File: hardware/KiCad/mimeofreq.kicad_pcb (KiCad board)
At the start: 4 copper layers, 60 x 70 mm, 45 parts, among them J1 AudioJack2, J2 AudioJack2, J3 Jack-DC, SW1 SW_SPST, SW2 SW_SPST, SW3 SW_SPDT, U1 MCP6022, U2 MCP6022

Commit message: Adding op amps to board; bypass cap correction.
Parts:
- moved C8 106.3 mm to (151.0, 85.2)
- moved U2 98.6 mm to (140.2, 85.2)
- moved U1 87.9 mm to (140.2, 63.7)
- moved C4 85.4 mm to (151.0, 63.7)
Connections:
- C4 pad 2: Net-(U1C-V+) -> GND
- C8 pad 2: Net-(U2C-V+) -> GND
- U1 pad 8: Net-(U1C-V+) -> +3V3
- U2 pad 8: Net-(U2C-V+) -> +3V3
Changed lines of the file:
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@@
 	(footprint "Capacitor_THT_Custom:C_Rect_L4.0mm_W2.6mm_P2.50mm"
 		(layer "F.Cu")
-		(at 52.7941 125.9156)
+		(at 151 85.19)
 		(descr "C, Rect series, Radial; Designed for K104x15X7RF5xxx 0.1uF X7R ceramic capacitor.")
 		(tags "K104K15X7RF5TL2 ")
@@
 			(layers "*.Cu" "*.Mask")
 			(remove_unused_layers no)
-			(net "Net-(U2C-V+)")
+			(net "GND")
 			(pintype "passive")
 		)
@@
 	(footprint "Package_DIP:DIP-8_W7.62mm"
 		(layer "F.Cu")
-		(at 71.225 118.175)
+		(at 140.195 63.69)
 		(descr "8-lead though-hole mounted DIP package, row spacing 7.62mm (300 mils)")
 		(tags "THT DIP DIL PDIP 2.54mm 7.62mm 300mil")
@@
 		)
 		(point
-			(at 75.035 121.985)
+			(at 144.005 67.5)
 			(size 1.27)
 			(layer "F.Fab")
@@
 			(layers "*.Cu" "*.Mask")
 			(remove_unused_layers no)
-			(net "Net-(U1C-V+)")
+			(net "+3V3")
 			(pinfunction "V+_8")
 			(pintype "power_in")
@@
 	(footprint "Capacitor_THT_Custom:C_Rect_L4.0mm_W2.6mm_P2.50mm"
 		(layer "F.Cu")
-		(at 76.8641 106.1056)
+		(at 151 63.7)
 		(descr "C, Rect series, Radial; Designed for K104x15X7RF5xxx 0.1uF X7R ceramic capacitor.")
 		(tags "K104K15X7RF5TL2 ")
@@
 			(layers "*.Cu" "*.Mask")
 			(remove_unused_layers no)
-			(net "Net-(U1C-V+)")
+			(net "GND")
 			(pintype "passive")
 		)
@@
 	(footprint "Package_DIP:DIP-8_W7.62mm"
 		(layer "F.Cu")
-		(at 43.855 106.025)
+		(at 140.195 85.19)
 		(descr "8-lead though-hole mounted DIP package, row spacing 7.62mm (300 mils)")
 		(tags "THT DIP DIL PDIP 2.54mm 7.62mm 300mil")
@@
 		)
 		(point
-			(at 47.665 109.835)
+			(at 144.005 89)
 			(size 1.27)
 			(layer "F.Fab")
@@
 			(layers "*.Cu" "*.Mask")
 			(remove_unused_layers no)
-			(net "Net-(U2C-V+)")
+			(net "+3V3")
 			(pinfunction "V+_8")
 			(pintype "power_in")

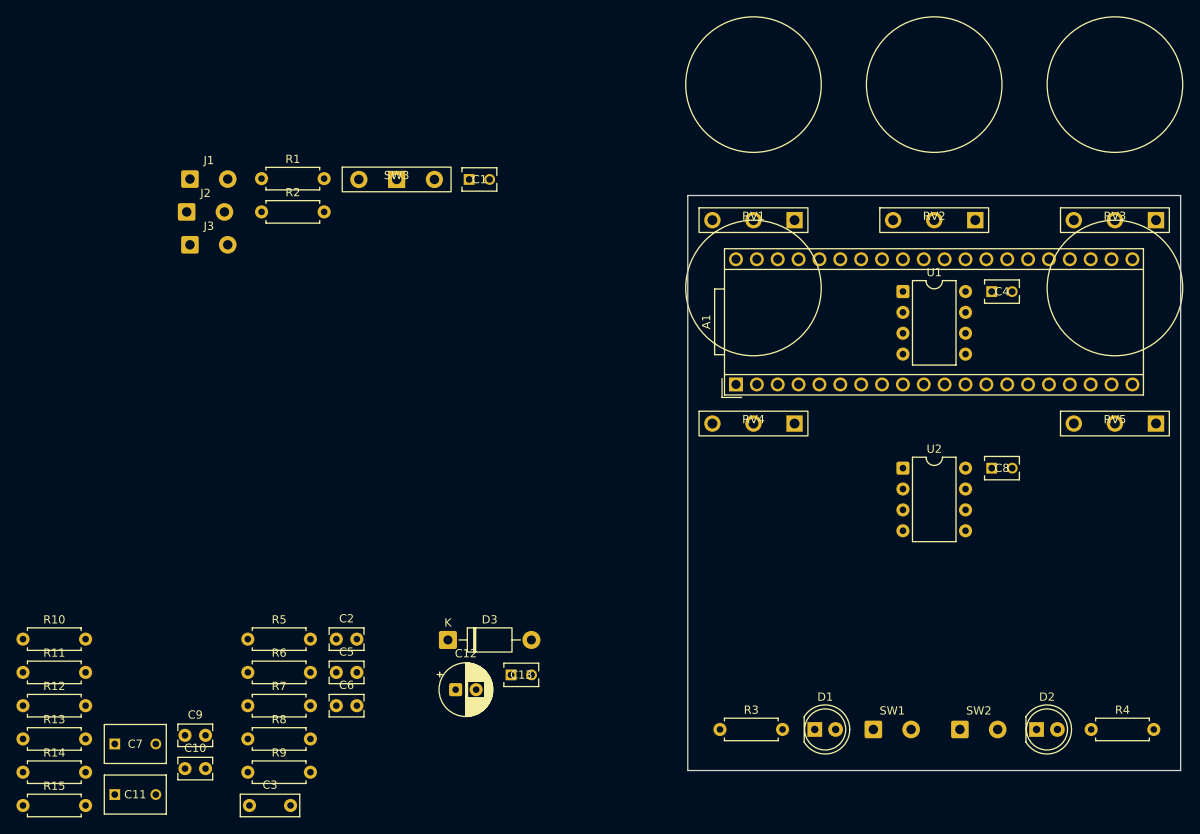
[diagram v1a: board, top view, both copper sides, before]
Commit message: Initial resistor board placement.
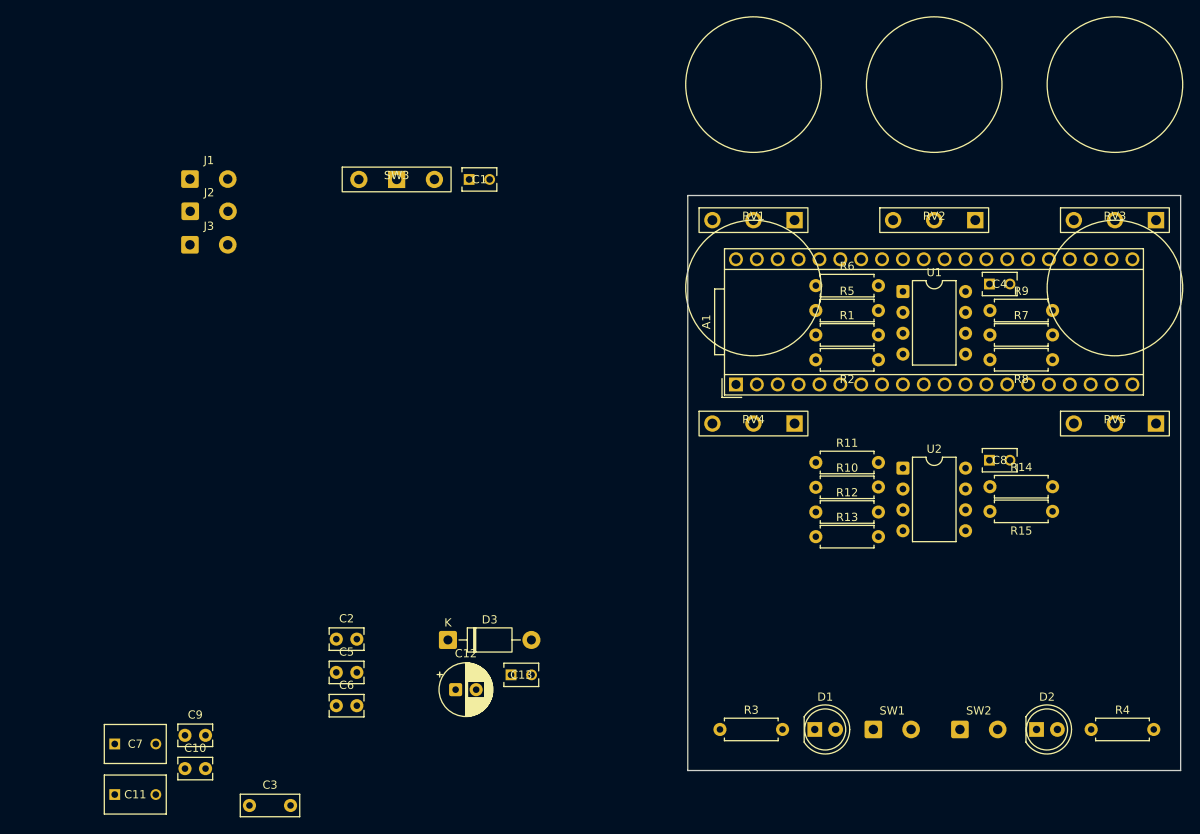
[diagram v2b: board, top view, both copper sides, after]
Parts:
- moved R15 130.3 mm to (158.4, 90.5), turned to 180 degrees
- moved R14 122.7 mm to (150.8, 87.5)
- moved R8 108.3 mm to (158.4, 72.0), turned to 180 degrees
- moved R9 106.4 mm to (150.8, 66.0)
- moved R7 101.0 mm to (150.8, 69.0)
- moved R11 99.8 mm to (129.6, 84.5)
- moved R13 99.6 mm to (129.6, 93.5)
- moved R12 99.4 mm to (129.6, 90.5)
- moved R10 98.3 mm to (129.6, 87.5)
- moved R6 83.7 mm to (129.6, 63.0)
- moved R5 79.9 mm to (129.6, 66.0)
- moved R2 77.2 mm to (137.2, 72.0), turned to 180 degrees
- moved R1 70.1 mm to (129.6, 69.0)
- moved C8 1.00 mm to (150.7, 84.2)
- moved C4 0.97 mm to (150.7, 62.8)
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
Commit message: All components fit on PCB. Some footprints replaced.
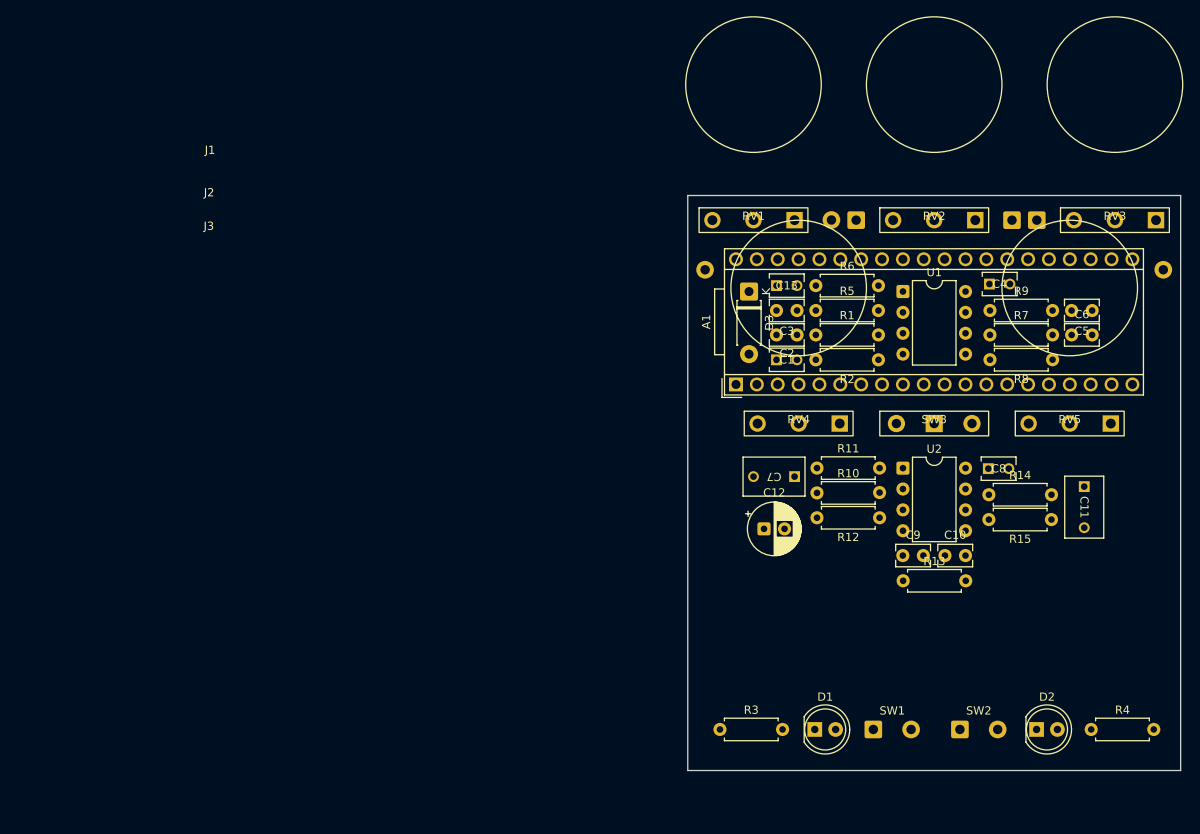
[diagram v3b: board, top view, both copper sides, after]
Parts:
- C3: footprint Capacitor_THT:C_Rect_L7.0mm_W2.5mm_P5.00mm -> Capacitor_THT:C_Rect_L4.0mm_W2.5mm_P2.50mm
- D3: footprint Diode_THT:D_DO-41_SOD81_P10.16mm_Horizontal -> Diode_THT:D_DO-41_SOD81_P7.62mm_Horizontal
- moved C11 123.8 mm to (162.3, 87.4), turned to -90 degrees
- moved C5 102.0 mm to (163.2, 66.0), turned to 180 degrees
- moved C6 100.3 mm to (160.7, 69.0)
- moved C10 96.1 mm to (145.3, 95.8)
- moved C9 90.1 mm to (140.2, 95.8)
- moved C3 89.9 mm to (127.3, 66.0), turned to 180 degrees
- moved C7 88.9 mm to (127.0, 86.2), turned to 180 degrees
- moved SW3 71.9 mm to (144.0, 79.8)
- moved C2 65.1 mm to (124.8, 69.0)
- moved C13 57.4 mm to (124.8, 63.0)
- moved D3 56.1 mm to (121.5, 63.7), turned to -90 degrees
- moved C1 43.4 mm to (124.8, 72.0)
- moved C12 42.3 mm to (123.3, 92.6)
- moved R13 11.9 mm to (140.2, 98.9)
- moved R12 7.79 mm to (137.3, 91.2), turned to 180 degrees
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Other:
- copper layers 4 -> 2

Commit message: Upper half initial routing.
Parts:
- moved R4 10.0 mm to (163.0, 107.0)
- moved D1 10.0 mm to (129.5, 107.0)
- moved D2 10.0 mm to (156.5, 107.0)
- moved R3 10.0 mm to (117.9, 107.0)
- moved SW1 10.0 mm to (136.6, 107.0)
- moved SW2 10.0 mm to (147.1, 107.0)
- moved R2 7.62 mm to (129.6, 72.0), turned to 0 degrees
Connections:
- A1 pad 22: /POT1 -> /POT5
- A1 pad 23: /POT2 -> /POT4
- A1 pad 25: /POT4 -> /POT2
- A1 pad 26: /POT5 -> /POT1
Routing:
- net +3V3: track 0.00 -> 189.2 mm
- net /POT4: track 0.00 -> 47.9 mm
- net +9VCLEAN: track 0.00 -> 45.6 mm
- net /POT1: track 0.00 -> 38.6 mm
- net +9V: track 0.00 -> 28.4 mm
- net /POT5: track 0.00 -> 22.1 mm
- net Net-(R6-Pad2): track 0.00 -> 16.8 mm
- net Net-(U1B-+): track 0.00 -> 16.7 mm
- net Net-(U1B--): track 0.00 -> 16.5 mm
- net /POT2: track 0.00 -> 15.9 mm
- net VGND: track 0.00 -> 14.2 mm
- net /Input Buffer/JACK_IN: track 0.00 -> 13.7 mm
- net Net-(U1A--): track 0.00 -> 12.0 mm
- net /IN: track 0.00 -> 9.75 mm
- net Net-(C5-Pad1): track 0.00 -> 9.07 mm
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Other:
- board size 60 x 70 mm -> 60 x 60 mm

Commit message: Full board initial routing.
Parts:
- moved D1 2.61 mm to (132.1, 107.0), turned to 180 degrees
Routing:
- net /LED2: track 0.00 -> 65.7 mm
- net /FS2: track 0.00 -> 55.1 mm
- net /OUT: track 0.00 -> 51.0 mm
- net /FS1: track 0.00 -> 44.6 mm
- net /Output Buffer/JACK_OUT: track 0.00 -> 39.8 mm
- net /LED1: track 0.00 -> 36.0 mm
- net VGND: track 14.2 -> 39.0 mm, vias 0 -> 2
- net Net-(C9-Pad1): track 0.00 -> 15.4 mm
- net Net-(U2B--): track 0.00 -> 13.4 mm
- net Net-(U2A--): track 0.00 -> 11.9 mm
- net Net-(R11-Pad2): track 0.00 -> 10.1 mm
- net Net-(U2B-+): track 0.00 -> 8.18 mm
- net +9VCLEAN: track 45.6 -> 41.0 mm, vias 0 -> 2
- net Net-(C11-Pad1): track 0.00 -> 4.40 mm
- net Net-(D2-A): track 0.00 -> 4.02 mm
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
